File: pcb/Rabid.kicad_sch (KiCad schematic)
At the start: 223 parts, among them J1 USB Connector, J3 GPIO Debug Header, SW1 Esc, SW10 A, SW100 Unused, SW101 Unused, SW102 →, SW103 BootSel, SW104 Reset, SW11 Z, SW12 LMeta, SW13 F1, SW14 2, SW15 W, SW16 S, SW17 X, SW18 LAlt, SW19 F2, SW2 Tilde, SW20 3, SW21 E, SW22 D, SW23 C, SW24 Unused, SW25 F3, SW26 4, SW27 R, SW28 F, SW29 V, SW3 Tab, SW30 Unused, SW31 F4, SW32 5, SW33 T, SW34 G, SW35 B, SW36 Unused, SW37 F5, SW38 6, SW39 Y, SW4 CapsLk, SW40 H, SW41 N, SW42 Space, SW43 F6, SW44 7, SW45 U, SW46 J, SW47 M, SW48 Unused, SW49 F7, SW5 LShift, SW50 8, SW51 I, SW52 K, SW53 ,, SW54 Unused, SW55 F8, SW56 9, SW57 O, SW58 L, SW59 ., SW6 LCtrl, SW60 Unused, SW61 F9, SW62 0, SW63 P, SW64 ;, SW65 /, SW66 AltGr, SW67 F10, SW68 -, SW69 [, SW7 Unused, SW70 ", SW71 RShift, SW72 RMeta, SW73 F11, SW74 =, SW75 ]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

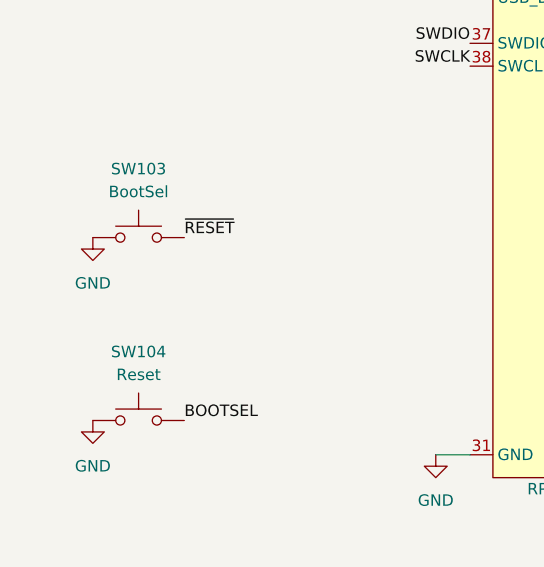
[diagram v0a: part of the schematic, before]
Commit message: PCB: Swap Reset and BootSel button silkscreens.
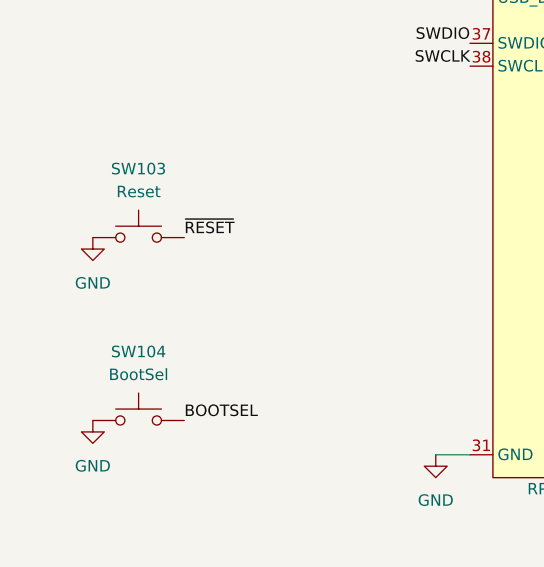
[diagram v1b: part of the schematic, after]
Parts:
- SW103: value BootSel -> Reset
- SW104: value Reset -> BootSel
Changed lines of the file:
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@@
     (in_bom yes) (on_board yes) (fields_autoplaced)
     (property "Reference" "SW104" (id 0) (at 33.02 245.11 0))
-    (property "Value" "Reset" (id 1) (at 33.02 247.65 0))
+    (property "Value" "BootSel" (id 1) (at 33.02 247.65 0))
     (property "Footprint" "Button_Switch_THT:SW_PUSH_6mm" (id 2) (at 33.02 247.65 0)
       (effects (font (size 1.27 1.27)) hide)
@@
     (in_bom yes) (on_board yes)
     (property "Reference" "SW103" (id 0) (at 33.02 224.79 0))
-    (property "Value" "BootSel" (id 1) (at 33.02 227.33 0))
+    (property "Value" "Reset" (id 1) (at 33.02 227.33 0))
     (property "Footprint" "Button_Switch_THT:SW_PUSH_6mm" (id 2) (at 33.02 227.33 0)
       (effects (font (size 1.27 1.27)) hide)
@@
     )
     (path "/cf26448c-5f86-443a-813f-8205ab4f6600"
-      (reference "SW103") (unit 1) (value "BootSel") (footprint "Button_Switch_THT:SW_PUSH_6mm")
+      (reference "SW103") (unit 1) (value "Reset") (footprint "Button_Switch_THT:SW_PUSH_6mm")
     )
     (path "/6df29cc0-92ba-4b02-9bf3-89ee5f38d720"
-      (reference "SW104") (unit 1) (value "Reset") (footprint "Button_Switch_THT:SW_PUSH_6mm")
+      (reference "SW104") (unit 1) (value "BootSel") (footprint "Button_Switch_THT:SW_PUSH_6mm")
     )
     (path "/192f83a9-3726-4136-83ac-7fa10874c246"
